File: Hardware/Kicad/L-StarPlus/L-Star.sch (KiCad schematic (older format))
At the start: 53 parts, among them IC1 24LC256, IC2 AS6C1008-55PCN (OPTIONAL), IC3 WDC 65C02, IC4 P8X32A, IC5 LM1086-5.0, IC6 LM1086-3.3, P1 PROP PLUG, P2 PS/2 KBD, P3 TV OUT, P4 POWER IN, P5 EXPANSION (OPT), P6 PROP PLUG, P7 RESET, P8 RESET6502, SW1 RESET, SW2 RESET6502, X1 5MHz

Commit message: Changes to schematic and PCB
Added mounting holes, deleted PCB shorts, deleted extra Prop plug header, changed OSHW logo to a dummy component on the schematic so it doesn't disappear when the netlist is re-imported into pcbnew
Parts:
- removed JP1: P26-KBDATA, 00Jac:00JG-SHORT, symbol 00JG-SHORT
- removed JP2: RDY, 00Jac:00JG-SHORT, symbol 00JG-SHORT
- removed JP3: ~IRQ, 00Jac:00JG-SHORT, symbol 00JG-SHORT
- removed JP4: ~NMI, 00Jac:00JG-SHORT, symbol 00JG-SHORT
- removed JP5: ~SO, 00Jac:00JG-SHORT, symbol 00JG-SHORT
- removed JP6: P27-KBCLK, 00Jac:00JG-SHORT, symbol 00JG-SHORT
- removed JP7: P25-TVOUT, 00Jac:00JG-SHORT, symbol 00JG-SHORT
- removed P6: PROP PLUG, Pin_Headers:Pin_Header_Straight_1x04, symbol CONN_4
- added U1: OSHW Logo, 00Jac:OSHW-logo_silkscreen-front_7mm, symbol Dummy
- added U2, U3, U4: Mount hole, 00Jac:MountHoleM3, symbol Dummy
- C6, C8: value 10u -> 47u
- C7: value 22u -> 47u
- R10, R11, R12, R13: value 3K3 OPT -> 3K3
- R9: value 82 -> 100
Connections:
- wire segments 308 -> 288
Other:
- note added: "For default configuration, place jumpers\non pins 1-2 on JP8, JP9, JP10 and JP11\n(RAM chip disabled, Propeller connected\nto TVOUT, KBDATA, KBCLK)"
- note removed: "JUMPER BLOCK\nAll jumpers are optional"
- moved on the sheet: C9, P1, P2, P3, P5, R4, R5, R6, R7, R8

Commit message: Changes to schematic and PCB design
Added support for 128K memory (A16 can be controlled by Propeller)
Updated documentation and footprint library from datasheets on Mouser.com
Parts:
- C1, C2, C3, C4, C5, C9: footprint Discret:C1 -> 00Jac:00JG-CapacitorMLCC
- IC5, IC6: footprint Transistors_TO-220:TO-220_Neutral123_Horizontal_LargePads -> 00Jac:00JG-TO-220_Neutral123_Horizontal_LargePads-Heatsink
- JP12: value RDY/~SO~/~SYNC~/~NMI~/~IRQ~/~RAMEN -> RDY/~SO~/~SYNC~/~NMI~/~IRQ~/A16/GND; footprint Pin_Headers:Pin_Header_Straight_1x06 -> Pin_Headers:Pin_Header_Straight_1x07; symbol CONN_01X06 -> CONN_01X07
- P2: footprint 00Jac:00JG-MD-60S -> 00Jac:00JG-MiniDin6
- P3: footprint 00Jac:00JG-RCJ-01X -> 00Jac:00JG-RCAsocket
- U1: footprint 00Jac:OSHW-logo_silkscreen-front_7mm -> 00Jac:00JG-OSHW-logo_silkscreen-front_7mm
- U2, U3, U4: footprint 00Jac:MountHoleM3 -> 00Jac:00JG-MountHoleM3
- X1: footprint Crystals:Crystal_HC49-U_Vertical -> 00Jac:00JG-Crystal_HC49-U_Vertical
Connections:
- net labels added: A16
- wire segments 288 -> 291
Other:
- note added: "For default configuration, place jumpers\non pins 1-2 on all jumpers\n(RAM chip disabled, Propeller connected\nto TVOUT, KBDATA, KBCLK).\nFor alternate configurations, place\njunmpers between jumper blocks\non pins 2-7."
- note removed: "For default configuration, place jumpers\non pins 1-2 on JP8, JP9, JP10 and JP11\n(RAM chip disabled, Propeller connected\nto TVOUT, KBDATA, KBCLK)"

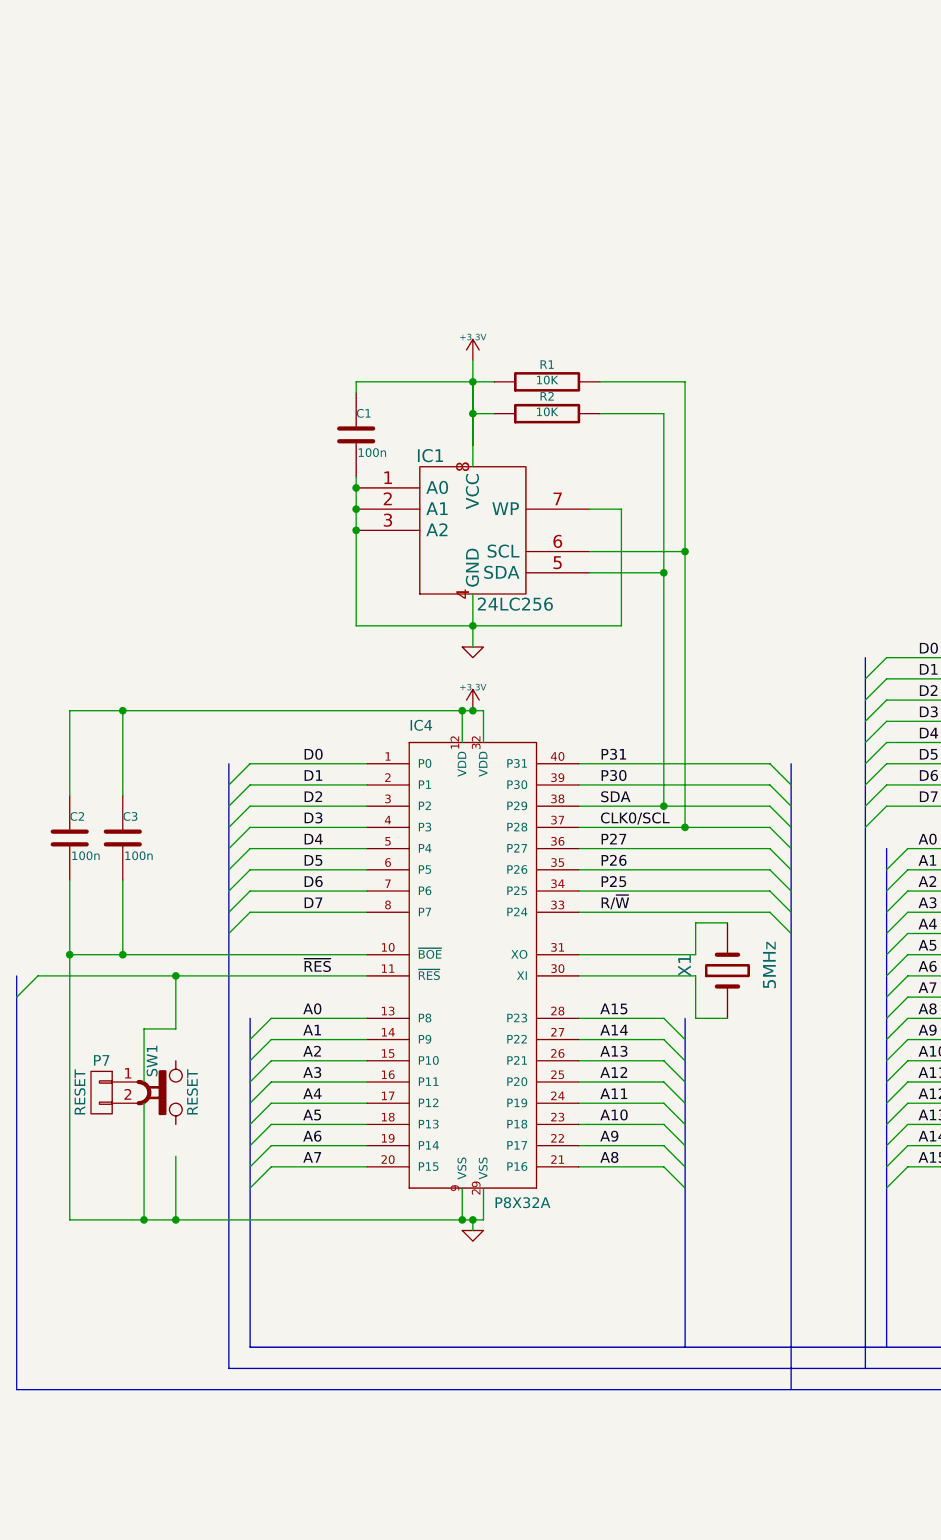
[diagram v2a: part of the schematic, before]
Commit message: Adding missing pull-up resistors to P31 and Reset
This makes it possible to run L-Star without Prop-Plug. Thanks cbmeeks for your help!
Also made some small layout changes in schematic and PCB and updated copyright year.
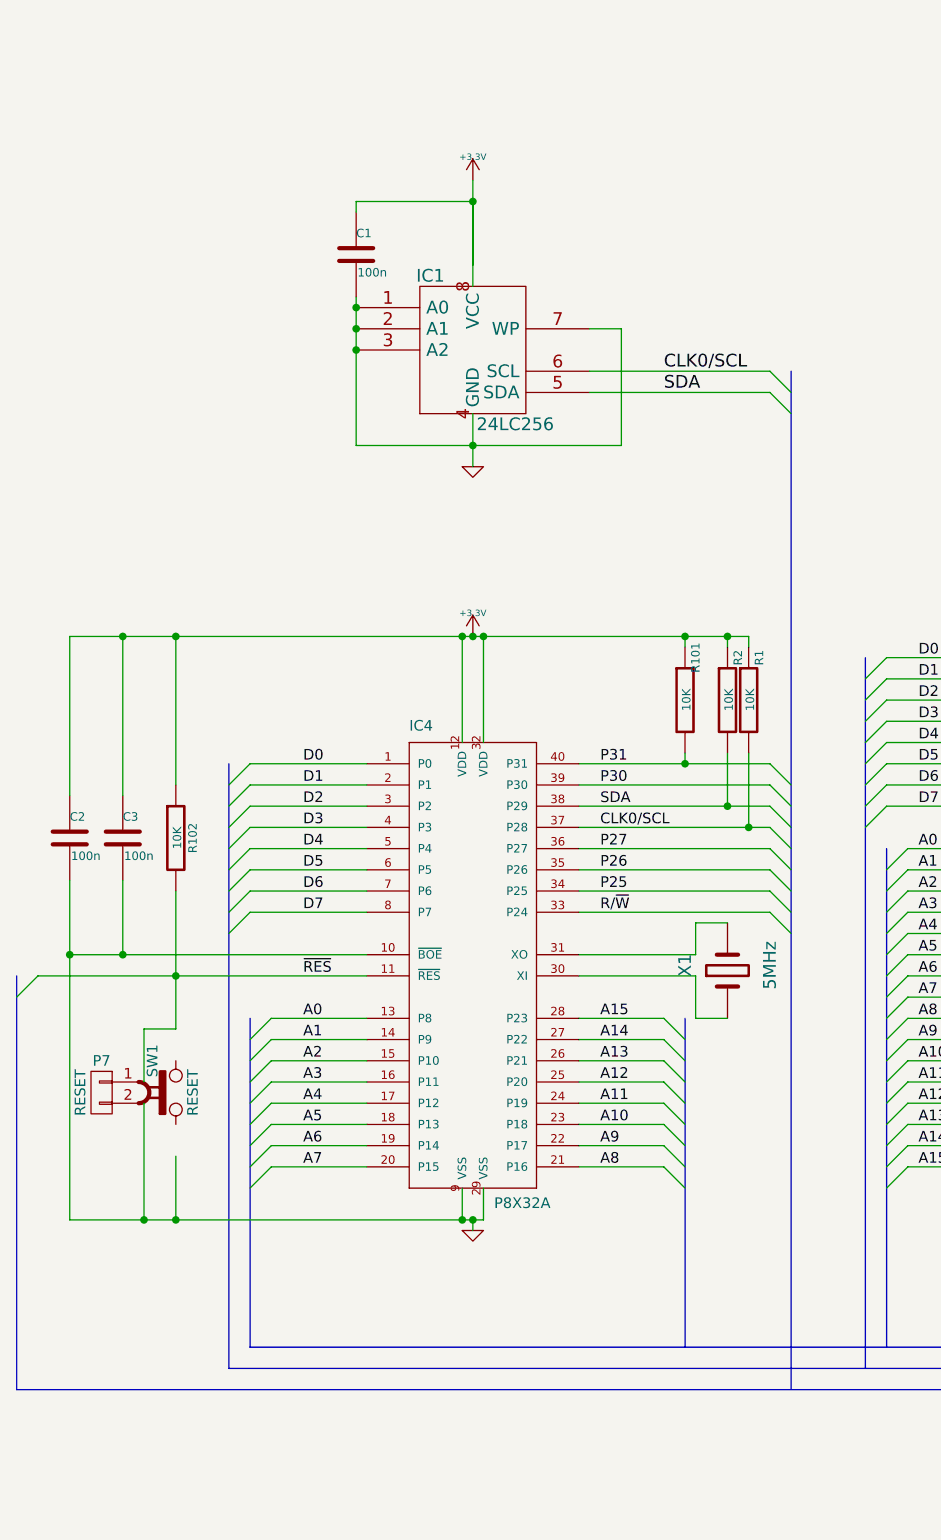
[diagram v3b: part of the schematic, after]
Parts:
- added R101, R102: 10K, Discret:R3, symbol R
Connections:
- net +3V3: now also R101.1, R102.1
- net P31: now also R101.2
- net ~RES: now also R102.2
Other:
- moved on the sheet: C1, IC1, R1, R2
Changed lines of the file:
@@
 Sheet 1 1
 Title "L-Star"
-Date "30 January 2015"
+Date "2016-02-14"
 Rev "2"
-Comp "(C) 2015 Jac Goudsmit"
+Comp "(C) 2016 Jac Goudsmit"
 Comment1 "Simplified Software-Defined 6502 Computer"
 Comment2 "https://github.com/JacGoudsmit/L-Star"
@@
 L GND #PWR09
 U 1 1 547A8E00
-P 2950 4050
-F 0 "#PWR09" H 2950 4050 30  0001 C CNN
-F 1 "GND" H 2950 3980 30  0001 C CNN
-F 2 "" H 2950 4050 60  0000 C CNN
-F 3 "" H 2950 4050 60  0000 C CNN
-	1    2950 4050
+P 2950 3200
+F 0 "#PWR09" H 2950 3200 30  0001 C CNN
+F 1 "GND" H 2950 3130 30  0001 C CNN
+F 2 "" H 2950 3200 60  0000 C CNN
+F 3 "" H 2950 3200 60  0000 C CNN
+	1    2950 3200
 	1    0    0    -1
 $EndComp
@@
 L R R2
 U 1 1 547A8E06
-P 3300 2950
-F 0 "R2" V 3380 2950 40  0000 C CNN
-F 1 "10K" V 3307 2951 40  0000 C CNN
-F 2 "Discret:R3" V 3230 2950 30  0001 C CNN
-F 3 "~" H 3300 2950 30  0000 C CNN
-	1    3300 2950
-	0    -1   -1   0
+P 4150 4300
+F 0 "R2" V 4200 4500 40  0000 C CNN
+F 1 "10K" V 4157 4301 40  0000 C CNN
+F 2 "Discret:R3" V 4080 4300 30  0001 C CNN
+F 3 "~" H 4150 4300 30  0000 C CNN
+	1    4150 4300
+	1    0    0    -1
 $EndComp
 $Comp
@@
 L C C1
 U 1 1 547A8E12
-P 2400 3050
-F 0 "C1" H 2400 3150 40  0000 L CNN
-F 1 "100n" H 2406 2965 40  0000 L CNN
-F 2 "00Jac:00JG-CapacitorMLCC" H 2438 2900 30  0001 C CNN
-F 3 "~" H 2400 3050 60  0000 C CNN
-	1    2400 3050
+P 2400 2200
+F 0 "C1" H 2400 2300 40  0000 L CNN
+F 1 "100n" H 2406 2115 40  0000 L CNN
+F 2 "00Jac:00JG-CapacitorMLCC" H 2438 2050 30  0001 C CNN
+F 3 "~" H 2400 2200 60  0000 C CNN
+	1    2400 2200
 	1    0    0    -1
 $EndComp
@@
 L 24LC IC1
 U 1 1 547A8E24
-P 2950 3500
-F 0 "IC1" H 2750 3850 60  0000 C CNN
-F 1 "24LC256" H 3150 3150 60  0000 C CNN
-F 2 "Sockets_DIP:DIP-8__300" H 2950 3500 60  0001 C CNN
-F 3 "" H 2950 3500 60  0000 C CNN
-	1    2950 3500
+P 2950 2650
+F 0 "IC1" H 2750 3000 60  0000 C CNN
+F 1 "24LC256" H 3150 2300 60  0000 C CNN
+F 2 "Sockets_DIP:DIP-8__300" H 2950 2650 60  0001 C CNN
+F 3 "" H 2950 2650 60  0000 C CNN
+	1    2950 2650
 	1    0    0    -1
 $EndComp
@@
 L +3.3V #PWR010
 U 1 1 547A8E83
-P 2950 4350
-F 0 "#PWR010" H 2950 4310 30  0001 C CNN
-F 1 "+3.3V" H 2950 4460 30  0000 C CNN
-F 2 "" H 2950 4350 60  0000 C CNN
-F 3 "" H 2950 4350 60  0000 C CNN
-	1    2950 4350
+P 2950 4000
+F 0 "#PWR010" H 2950 3960 30  0001 C CNN
+F 1 "+3.3V" H 2950 4110 30  0000 C CNN
+F 2 "" H 2950 4000 60  0000 C CNN
+F 3 "" H 2950 4000 60  0000 C CNN
+	1    2950 4000
 	1    0    0    -1
 $EndComp
@@
 L +3.3V #PWR011
 U 1 1 547A8E89
-P 2950 2700
-F 0 "#PWR011" H 2950 2660 30  0001 C CNN
-F 1 "+3.3V" H 2950 2810 30  0000 C CNN
-F 2 "" H 2950 2700 60  0000 C CNN
-F 3 "" H 2950 2700 60  0000 C CNN
-	1    2950 2700
+P 2950 1850
+F 0 "#PWR011" H 2950 1810 30  0001 C CNN
+F 1 "+3.3V" H 2950 1960 30  0000 C CNN
+F 2 "" H 2950 1850 60  0000 C CNN
+F 3 "" H 2950 1850 60  0000 C CNN
+	1    2950 1850
 	1    0    0    -1
 $EndComp
@@
 L R R1
 U 1 1 547A8E91
-P 3300 2800
-F 0 "R1" V 3380 2800 40  0000 C CNN
-F 1 "10K" V 3307 2801 40  0000 C CNN
-F 2 "Discret:R3" V 3230 2800 30  0001 C CNN
-F 3 "~" H 3300 2800 30  0000 C CNN
-	1    3300 2800
-	0    -1   -1   0
+P 4250 4300
+F 0 "R1" V 4300 4500 40  0000 C CNN
+F 1 "10K" V 4257 4301 40  0000 C CNN
+F 2 "Discret:R3" V 4180 4300 30  0001 C CNN
+F 3 "~" H 4250 4300 30  0000 C CNN
+	1    4250 4300
+	1    0    0    -1
 $EndComp
 $Comp
@@
 	900  5600 2450 5600
 Wire Wire Line
-	1550 5850 1550 5600
+	1550 5200 1550 5850
 Wire Wire Line
 	1550 6750 1550 6450
@@
 	1050 5500 2450 5500
 Wire Wire Line
-	2950 2700 2950 3100
-Wire Wire Line
-	2950 2800 2950 3200
-Wire Wire Line
-	2950 3800 2950 4050
-Wire Wire Line
-	2400 3250 2400 3950
-Connection ~ 2400 3400
-Connection ~ 2950 3950
-Connection ~ 2400 3500
-Wire Wire Line
-	3650 3400 3500 3400
-Wire Wire Line
-	3650 3950 3650 3400
-Wire Wire Line
-	2400 2800 3050 2800
-Connection ~ 2950 2800
-Wire Wire Line
-	3500 3600 3950 3600
-Wire Wire Line
-	3500 3700 3850 3700
-Wire Wire Line
-	3850 2950 3850 4800
-Connection ~ 3850 3700
-Wire Wire Line
-	2900 4350 2900 4500
-Connection ~ 2950 4350
+	2950 1850 2950 2250
+Wire Wire Line
+	2950 1950 2950 2350
+Wire Wire Line
+	2950 2950 2950 3200
+Wire Wire Line
+	2400 2400 2400 3100
+Connection ~ 2400 2550
+Connection ~ 2950 3100
+Connection ~ 2400 2650
+Wire Wire Line
+	3650 2550 3500 2550
+Wire Wire Line
+	3650 3100 3650 2550
+Wire Wire Line
+	3500 2750 4350 2750
+Wire Wire Line
+	3500 2850 4350 2850
+Wire Wire Line
+	2900 4000 2900 4500
+Connection ~ 2950 4000
 Wire Wire Line
 	2900 6750 2900 6600
 Wire Wire Line
-	1300 4750 1300 4350
-Wire Wire Line
-	1050 4350 3000 4350
-Connection ~ 2900 4350
-Wire Wire Line
-	3000 4350 3000 4500
+	1300 4750 1300 4000
+Wire Wire Line
+	1050 4000 4250 4000
+Connection ~ 2900 4000
+Wire Wire Line
+	3000 4000 3000 4500
 Wire Wire Line
 	4150 5350 4000 5350
@@
 	3450 5600 4000 5600
 Wire Wire Line
-	1050 4350 1050 4750
-Connection ~ 1300 4350
+	1050 4000 1050 4750
+Connection ~ 1300 4000
 Wire Wire Line
 	1050 5150 1050 6750
@@
 	1050 6750 3000 6750
 Wire Wire Line
-	2400 2800 2400 2850
-Wire Wire Line
-	2400 3950 3650 3950
-Connection ~ 2400 3300
+	2400 1950 2400 2000
+Wire Wire Line
+	2400 3100 3650 3100
+Connection ~ 2400 2450
 Wire Wire Line
 	3000 6750 3000 6600
@@
 	4000 5800 4150 5800
 Wire Wire Line
-	3850 2950 3550 2950
-Wire Wire Line
-	3950 2800 3950 4900
-Connection ~ 3950 3600
-Wire Wire Line
 	5950 3350 5950 4000
 Wire Wire Line
@@
 	7800 4100 7800 7550
 Wire Bus Line
-	4450 4600 4450 7550
+	4450 2750 4450 7550
 Wire Wire Line
 	3450 5300 4350 5300
@@
 Wire Wire Line
 	5950 6900 7650 6900
-Connection ~ 3950 4900
-Wire Wire Line
-	3550 2800 3950 2800
-Wire Wire Line
-	3050 2950 2950 2950
-Connection ~ 2950 2950
+Connection ~ 4250 4900
 Connection ~ 1550 6750
 Wire Wire Line
@@
 Wire Wire Line
 	3450 4700 4350 4700
-Connection ~ 3850 4800
+Connection ~ 4150 4800
 Wire Bus Line
 	800  5600 800  7550
@@
 Wire Wire Line
 	13050 2000 13150 2000
+$Comp
+L R R102
+U 1 1 56C142C2
+P 1550 4950
+F 0 "R102" V 1630 4950 40  0000 C CNN
+F 1 "10K" V 1557 4951 40  0000 C CNN
+F 2 "Discret:R3" V 1480 4950 30  0001 C CNN
+F 3 "" H 1550 4950 30  0000 C CNN
+	1    1550 4950
+	1    0    0    -1
+$EndComp
+Wire Wire Line
+	1550 4700 1550 4000
+Connection ~ 1550 4000
+$Comp
+L R R101
+U 1 1 56C1F599
+P 3950 4300
+F 0 "R101" V 4000 4500 40  0000 C CNN
+F 1 "10K" V 3957 4301 40  0000 C CNN
+F 2 "Discret:R3" V 3880 4300 30  0001 C CNN
+F 3 "" H 3950 4300 30  0000 C CNN
+	1    3950 4300
+	1    0    0    -1
+$EndComp
+Wire Wire Line
+	3950 4550 3950 4600
+Connection ~ 3950 4600
+Connection ~ 3000 4000
+Wire Wire Line
+	4250 4000 4250 4050
+Wire Wire Line
+	4150 4550 4150 4800
+Wire Wire Line
+	4250 4550 4250 4900
+Entry Wire Line
+	4350 2750 4450 2850
+Entry Wire Line
+	4350 2850 4450 2950
+Wire Wire Line
+	2400 1950 2950 1950
+Connection ~ 2950 1950
+Text Label 3850 2750 0    60   ~ 0
+CLK0/SCL
+Text Label 3850 2850 0    60   ~ 0
+SDA
+Wire Wire Line
+	3950 4050 3950 4000
+Connection ~ 3950 4000
+Wire Wire Line
+	4150 4000 4150 4050
+Connection ~ 4150 4000
 $EndSCHEMATC

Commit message: Numerous minor changes to schematic and PCB
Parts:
- removed R14: 3K3, Discret:R3, symbol R
- C5: value 100n (OPTIONAL) -> 100n
- C9: value 470p (OPT) -> 470p
- IC1: value 24LC256 -> 24LC512
- IC2: value AS6C1008-55PCN (OPTIONAL) -> AS6C1008-55PCN
- P5: value EXPANSION (OPT) -> EXPANSION
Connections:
- net BE is gone; now on net +3.3V: IC3.36 (NC(BE))
- net A11: now also IC2.23 (A10); no longer IC2.31 (A15)
- net A15: now also IC2.31 (A15); no longer IC2.23 (A10)
- net VSUPPLY: no longer names the net of C6.1, IC5.3 (VIN), P4.1
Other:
- note added: "For default configuration, place jumpers on\npins 1-2 of all jumper blocks.\nThis disables the SRAM chip and connects the\nPropeller to P25=TVOUT, P26=KBDATA, P27=KBCLK.\nFor alternate configurations, place jumpers\nbetween jumper blocks on pins 2-7."
- note removed: "For default configuration, place jumpers\non pins 1-2 on all jumpers\n(RAM chip disabled, Propeller connected\nto TVOUT, KBDATA, KBCLK).\nFor alternate configurations, place\njunmpers between jumper blocks\non pins 2-7."

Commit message: Many small changes to L-Star Plus schematic and PCB
Including but not limited to:
- Updated my Kicad to 4.0.2.
- Removed long list of unneeded libraries
- Moved power LED to corner near Prop plug
- Added shorted header for optional power switch (Thanks CBMeeks!)
- Replaced "POWER IN" by declaration of safe voltages and currents
- Added voltages to electrolytical caps
- Removed +5V from jac.lib; it was causing a conflict. Not sure why it was in there in the first place anyway.
- Added 3V3, VIN and VSUPPLY to POWER netclass. 3V3 replaced "+3.3V" after I updated Kicad
- Updated dates on schematic and PCB sheets
- Minor changes to traces on PCB
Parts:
- added SW3: PWR SWITCH, 00Jac:00JG_SHORTED_Pin_Header_Straight_1x02, symbol SWITCH_01
- C6, C7, C8: value 47u -> 47u/16V
- P4: value POWER IN -> 7-15V 1-1.5A IN
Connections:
- net labels added: VIN, VSUPPLY
- net labels removed: +3,3V
- wire segments 290 -> 292
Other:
- moved on the sheet: P4

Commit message: Many more minor changes to schematic and PCB (no actual functual changes)
- Redrew several schematic symbols and footprints
- Changed resistor footprint to have pins 400mils apart to fit regular resistors slightly better
- Moved some parts around, most notably the resistor to the LED
- Renumbered all parts in the schematic
- Renamed "TV OUT" to "VIDEO OUT"
-
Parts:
- P6: renamed from P3; value TV OUT -> VIDEO OUT
- R1: renamed from R3; footprint Discret:R3 -> 00Jac:00JG-R400
- R10: renamed from R4; footprint Discret:R3 -> 00Jac:00JG-R400
- R11: renamed from R5; footprint Discret:R3 -> 00Jac:00JG-R400
- R12: renamed from R6; footprint Discret:R3 -> 00Jac:00JG-R400
- R13: renamed from R7; footprint Discret:R3 -> 00Jac:00JG-R400
- R14: renamed from R8; footprint Discret:R3 -> 00Jac:00JG-R400
- R15: renamed from R9; footprint Discret:R3 -> 00Jac:00JG-R400
- R2: renamed from R10; footprint Discret:R3 -> 00Jac:00JG-R400
- R3: renamed from R11; footprint Discret:R3 -> 00Jac:00JG-R400
- R4: renamed from R12; footprint Discret:R3 -> 00Jac:00JG-R400
- R5: renamed from R13; footprint Discret:R3 -> 00Jac:00JG-R400
- R6: renamed from R101; footprint Discret:R3 -> 00Jac:00JG-R400
- R7: renamed from R2; footprint Discret:R3 -> 00Jac:00JG-R400
- R8: renamed from R1; footprint Discret:R3 -> 00Jac:00JG-R400
- R9: renamed from R102; footprint Discret:R3 -> 00Jac:00JG-R400
- SW3: footprint 00Jac:00JG_SHORTED_Pin_Header_Straight_1x02 -> 00Jac:00JG-SHORTED_Pin_Header_Straight_1x02; symbol SWITCH_01 -> SPST
- renumbered C9 to C6, C6 to C7, C7 to C8, C8 to C9, JP8 to JP1, JP11 to JP2, JP9 to JP3, JP12 to JP4, JP10 to JP5, P5 to P2, P2 to P3, P7 to P4, P8 to P5, P4 to P7
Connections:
- wire segments 292 -> 294
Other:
- note added: "For "default" configuration, place jumpers between\npins 1-2 of all jumper blocks.\nThis disables the SRAM chip and connects the\nPropeller to P25=TVOUT, P26=KBDATA, P27=KBCLK."
- note removed: "For default configuration, place jumpers on\npins 1-2 of all jumper blocks.\nThis disables the SRAM chip and connects the\nPropeller to P25=TVOUT, P26=KBDATA, P27=KBCLK.\nFor alternate configurations, place jumpers\nbetween jumper blocks on pins 2-7."
- moved on the sheet: R7, R8, SW1
